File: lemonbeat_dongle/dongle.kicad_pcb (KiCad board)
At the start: 4 copper layers, 50 x 20 mm, 82 parts, among them J201 USB_A, J202 Prog, J203 u.FL, J301 SMA, SW201 SW_Push, U201 nRF52840, U301 Si4467, Y201 32MHz, Y202 32.768kHz, Y301 26MHz

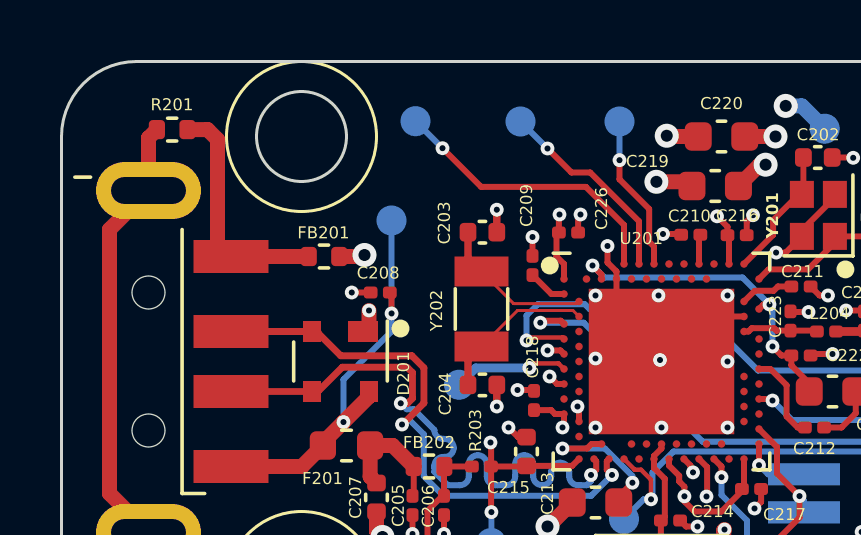
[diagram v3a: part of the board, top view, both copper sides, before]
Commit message: dongle: PCB: move test points away from hole
- move TP203 & TP206 away from hole (dongle & microjig)
- move TP205 away from TP206 (dongle & microjig)

Having the test points further away from the holes avoids shortcuts when
using a metal case & leaves space on the microjig for a nut.
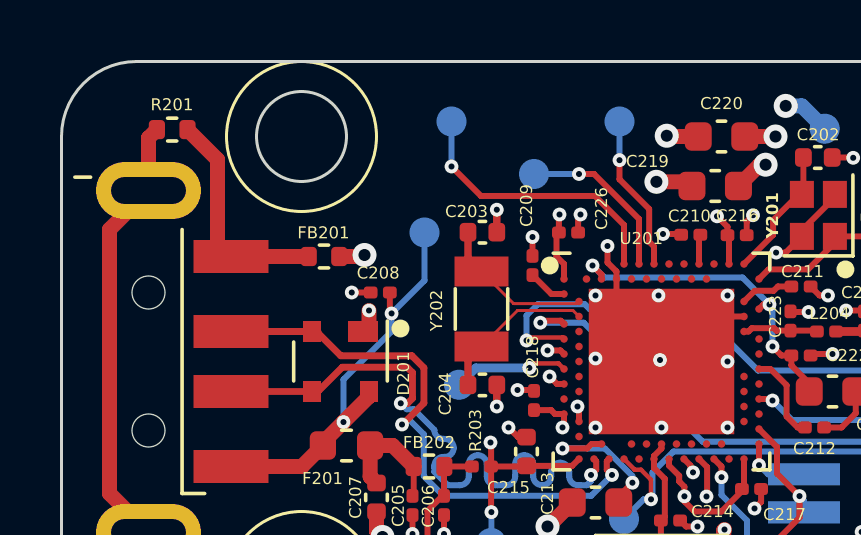
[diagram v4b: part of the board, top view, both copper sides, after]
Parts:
- moved TP205 1.81 mm to (126.2, 97.8)
- moved TP206 1.20 mm to (123.5, 96.0)
- moved TP203 1.17 mm to (122.6, 99.7)
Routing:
- net Net-(U201-AIN5/P0.29): track 6.75 -> 5.62 mm
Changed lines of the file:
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@@
     (property "ki_keywords" "cap capacitor")
     (attr smd)
-    (fp_text reference "C203" (at 1.27 0.31 270) (layer "F.SilkS")
+    (fp_text reference "C203" (at 0.53 0.69) (layer "F.SilkS")
         (effects (font (size 0.4 0.4) (thickness 0.1)))
     )
@@
   )
   (footprint "TestPoint:TestPoint_Pad_D1.0mm" (layer "B.Cu")
-    (at 125.8 96 180)
+    (at 126.25 97.75 180)
     (descr "SMD pad as test Point, diameter 1.0mm")
     (tags "test point SMD pad")
@@
   )
   (footprint "TestPoint:TestPoint_Pad_D1.0mm" (layer "B.Cu")
-    (at 121.5 99.3 180)
+    (at 122.6 99.7 180)
     (descr "SMD pad as test Point, diameter 1.0mm")
     (tags "test point SMD pad")
@@
   )
   (footprint "TestPoint:TestPoint_Pad_D1.0mm" (layer "B.Cu")
-    (at 122.3 95.99 180)
+    (at 123.5 96 180)
     (descr "SMD pad as test Point, diameter 1.0mm")
     (tags "test point SMD pad")
@@
   (segment (start 120.75 105) (end 120.75 105.167408) (width 0.5) (layer "F.Cu") (net 8))
   (segment (start 116.35 107.5) (end 118.5125 107.5) (width 0.5) (layer "F.Cu") (net 8))
-  (segment (start 121.502085 101.862085) (end 121.39 101.75) (width 0.2) (layer "F.Cu") (net 8))
-  (segment (start 121.502085 102.397915) (end 121.502085 101.862085) (width 0.2) (layer "F.Cu") (net 8))
   (segment (start 120.75 105.167408) (end 119.89912 106.018288) (width 0.5) (layer "F.Cu") (net 8))
   (segment (start 119.2125 106.704908) (end 119.89912 106.018288) (width 0.5) (layer "F.Cu") (net 8))
   (segment (start 118.5125 107.5) (end 119.2125 106.8) (width 0.5) (layer "F.Cu") (net 8))
+  (segment (start 121.445 101.7) (end 121.445 102.34083) (width 0.2) (layer "F.Cu") (net 8))
+  (segment (start 121.445 102.34083) (end 121.502085 102.397915) (width 0.2) (layer "F.Cu") (net 8))
   (via (at 119.89912 106.018288) (size 0.46) (drill 0.2) (layers "F.Cu" "B.Cu") (net 8))
   (via (at 121.502085 102.397915) (size 0.46) (drill 0.2) (layers "F.Cu" "B.Cu") (net 8))
-  (segment (start 121.502085 102.397915) (end 121.502085 102.997915) (width 0.2) (layer "B.Cu") (net 8))
-  (segment (start 119.89912 104.60088) (end 119.89912 106.018288) (width 0.2) (layer "B.Cu") (net 8))
   (segment (start 121.502085 102.997915) (end 119.89912 104.60088) (width 0.2) (layer "B.Cu") (net 8))
-  (segment (start 121.5 102.39583) (end 121.5 99.3) (width 0.2) (layer "B.Cu") (net 8))
-  (segment (start 121.502085 102.397915) (end 121.5 102.39583) (width 0.2) (layer "B.Cu") (net 8))
+  (segment (start 121.502085 102.997915) (end 121.502085 102.397915) (width 0.2) (layer "B.Cu") (net 8))
+  (segment (start 121.502085 102.397915) (end 122.6 101.3) (width 0.2) (layer "B.Cu") (net 8))
+  (segment (start 119.89912 104.60088) (end 119.89912 106.018288) (width 0.2) (layer "B.Cu") (net 8))
+  (segment (start 122.6 101.3) (end 122.6 99.7) (width 0.2) (layer "B.Cu") (net 8))
   (segment (start 126.83 101.75) (end 126.2 101.12) (width 0.2) (layer "F.Cu") (net 9))
   (segment (start 127.25 101.75) (end 126.83 101.75) (width 0.2) (layer "F.Cu") (net 9))
@@
   (segment (start 144.5375 111.4) (end 144.5375 110.2725) (width 0.2) (layer "F.Cu") (net 33))
   (segment (start 144.5375 110.2725) (end 144.9 109.91) (width 0.2) (layer "F.Cu") (net 33))
-  (segment (start 114.7 96.27) (end 115.37 96.27) (width 0.5) (layer "F.Cu") (net 34))
-  (segment (start 116.35 100.5) (end 118.1 100.5) (width 0.5) (layer "F.Cu") (net 34))
   (segment (start 115.7 100.05) (end 116.15 100.5) (width 0.5) (layer "F.Cu") (net 34))
-  (segment (start 115.7 96.6) (end 115.7 100.05) (width 0.5) (layer "F.Cu") (net 34))
-  (segment (start 115.37 96.27) (end 115.7 96.6) (width 0.5) (layer "F.Cu") (net 34))
+  (segment (start 116.35 100.5) (end 118.1 100.5) (width 0.5) (layer "F.Cu") (net 34))
+  (segment (start 115.7 97.27) (end 115.7 100.05) (width 0.5) (layer "F.Cu") (net 34))
   (segment (start 118.1 100.5) (end 118.74 100.5) (width 0.5) (layer "F.Cu") (net 34))
+  (segment (start 114.7 96.27) (end 115.7 97.27) (width 0.5) (layer "F.Cu") (net 34))
   (segment (start 112.1 99.6) (end 113.4 98.3) (width 0.5) (layer "F.Cu") (net 35))
   (segment (start 113.4 109.7) (end 112.1 108.4) (width 0.5) (layer "F.Cu") (net 35))
@@
   (segment (start 129.1 97.29) (end 129.1 96) (width 0.2) (layer "B.Cu") (net 48))
   (segment (start 129.75 99.327552) (end 129.75 100.75) (width 0.2) (layer "F.Cu") (net 49))
-  (segment (start 128.122448 97.7) (end 129.75 99.327552) (width 0.2) (layer "F.Cu") (net 49))
-  (segment (start 126.7 96.9) (end 127.5 97.7) (width 0.2) (layer "F.Cu") (net 49))
-  (segment (start 127.5 97.7) (end 128.122448 97.7) (width 0.2) (layer "F.Cu") (net 49))
-  (via (at 126.7 96.9) (size 0.46) (drill 0.2) (layers "F.Cu" "B.Cu") (net 49))
-  (segment (start 126.7 96.9) (end 125.8 96) (width 0.2) (layer "B.Cu") (net 49))
+  (segment (start 129.75 99.25) (end 128.25 97.75) (width 0.2) (layer "F.Cu") (net 49))
+  (segment (start 129.75 99.327552) (end 129.75 99.25) (width 0.2) (layer "F.Cu") (net 49))
+  (segment (start 128.25 97.75) (end 127.75 97.75) (width 0.2) (layer "F.Cu") (net 49))
+  (via (at 127.75 97.75) (size 0.46) (drill 0.2) (layers "F.Cu" "B.Cu") (net 49))
+  (segment (start 127.75 97.75) (end 126.25 97.75) (width 0.2) (layer "B.Cu") (net 49))
   (segment (start 129.25 99.45) (end 129.25 100.75) (width 0.2) (layer "F.Cu") (net 50))
-  (segment (start 127.98 98.18) (end 129.25 99.45) (width 0.2) (layer "F.Cu") (net 50))
-  (segment (start 123.2 96.89) (end 124.49 98.18) (width 0.2) (layer "F.Cu") (net 50))
-  (segment (start 124.49 98.18) (end 127.98 98.18) (width 0.2) (layer "F.Cu") (net 50))
-  (via (at 123.2 96.89) (size 0.46) (drill 0.2) (layers "F.Cu" "B.Cu") (net 50))
-  (segment (start 123.2 96.89) (end 122.3 95.99) (width 0.2) (layer "B.Cu") (net 50))
+  (segment (start 124.483 98.483) (end 123.5 97.5) (width 0.2) (layer "F.Cu") (net 50))
+  (segment (start 128.283 98.483) (end 124.483 98.483) (width 0.2) (layer "F.Cu") (net 50))
+  (segment (start 129.25 99.45) (end 128.283 98.483) (width 0.2) (layer "F.Cu") (net 50))
+  (via (at 123.5 97.5) (size 0.46) (drill 0.2) (layers "F.Cu" "B.Cu") (net 50))
+  (segment (start 123.5 97.5) (end 123.5 96) (width 0.2) (layer "B.Cu") (net 50))
   (segment (start 141.7875 106.375) (end 141.221 106.375) (width 0.2) (layer "F.Cu") (net 86))
   (segment (start 140.373 107.223) (end 140.373 108.923) (width 0.2) (layer "F.Cu") (net 86))

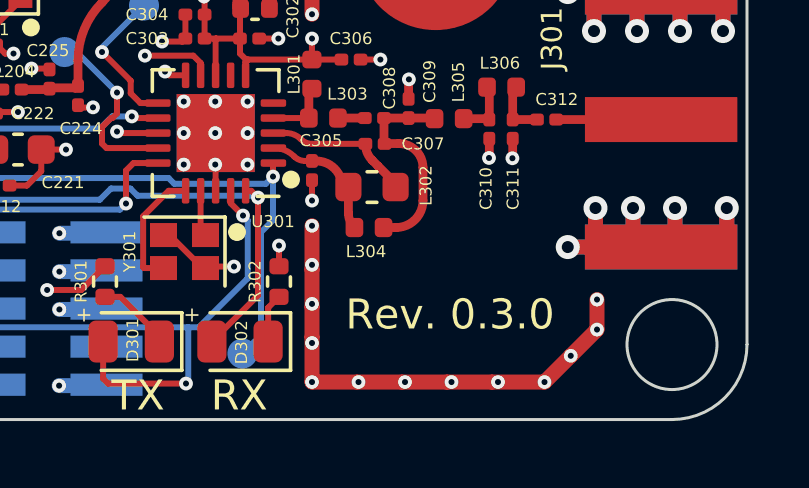
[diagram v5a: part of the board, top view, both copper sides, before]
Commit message: dongle & micro jig: increase revision to 0.4.0 everywhere
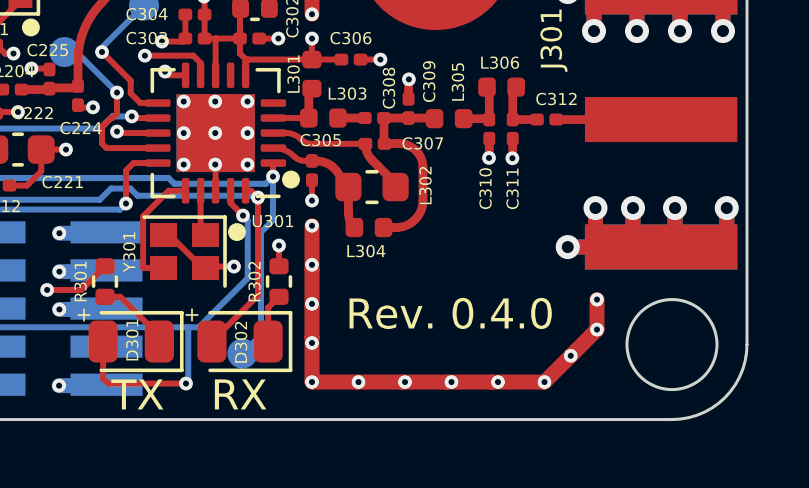
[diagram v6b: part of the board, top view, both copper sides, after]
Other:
- board text added: "Rev. 0.4.0"
- board text removed: "Rev. 0.3.0"
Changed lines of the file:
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@@
     (effects (font (size 0.5 0.5) (thickness 0.1)))
   )
-  (gr_text "Rev. 0.3.0" (at 150.6 110.5) (layer "F.SilkS")
+  (gr_text "Rev. 0.4.0" (at 150.6 110.5) (layer "F.SilkS")
     (effects (font (size 1 1) (thickness 0.15)))
   )

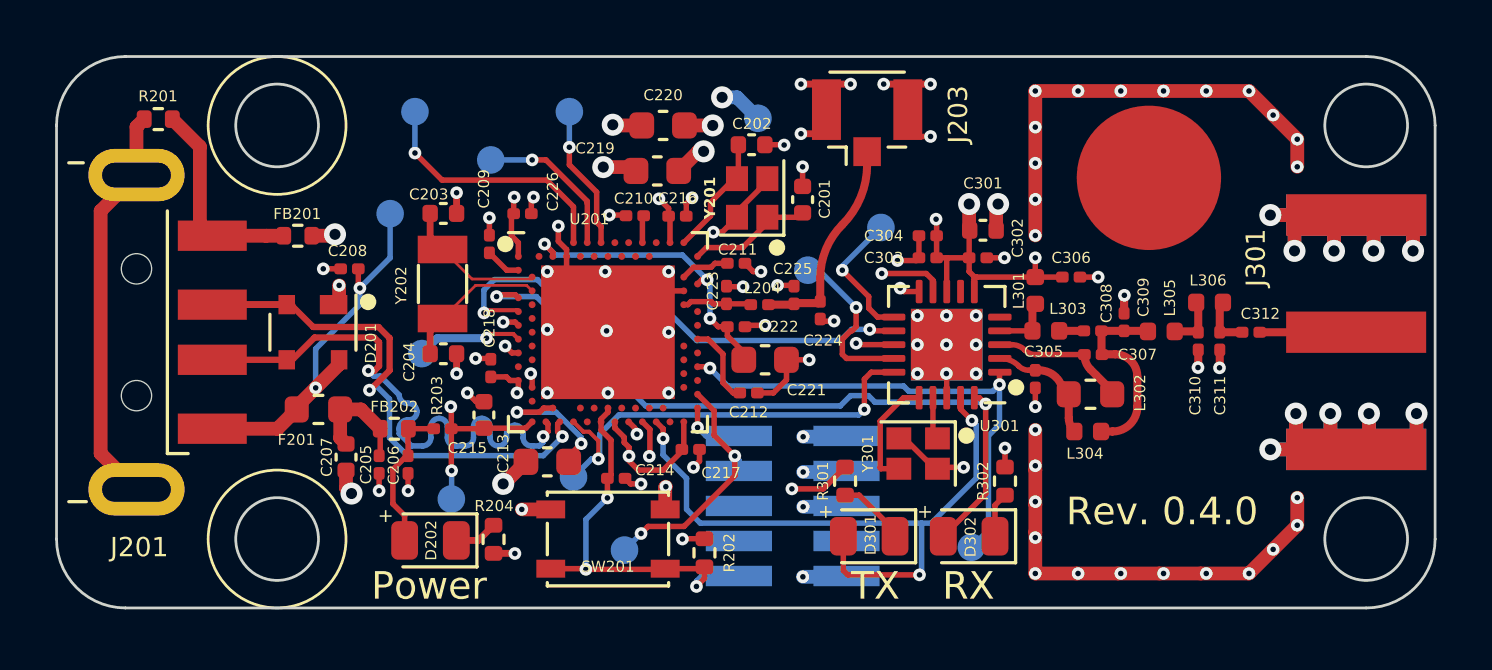
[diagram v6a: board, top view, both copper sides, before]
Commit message: dongle: schematic & PCB: add button
The existing button is connected to reset. This adds a second button
connected to P1.15, which can be used for user input (e.g. to enter the
boot loader on power on).
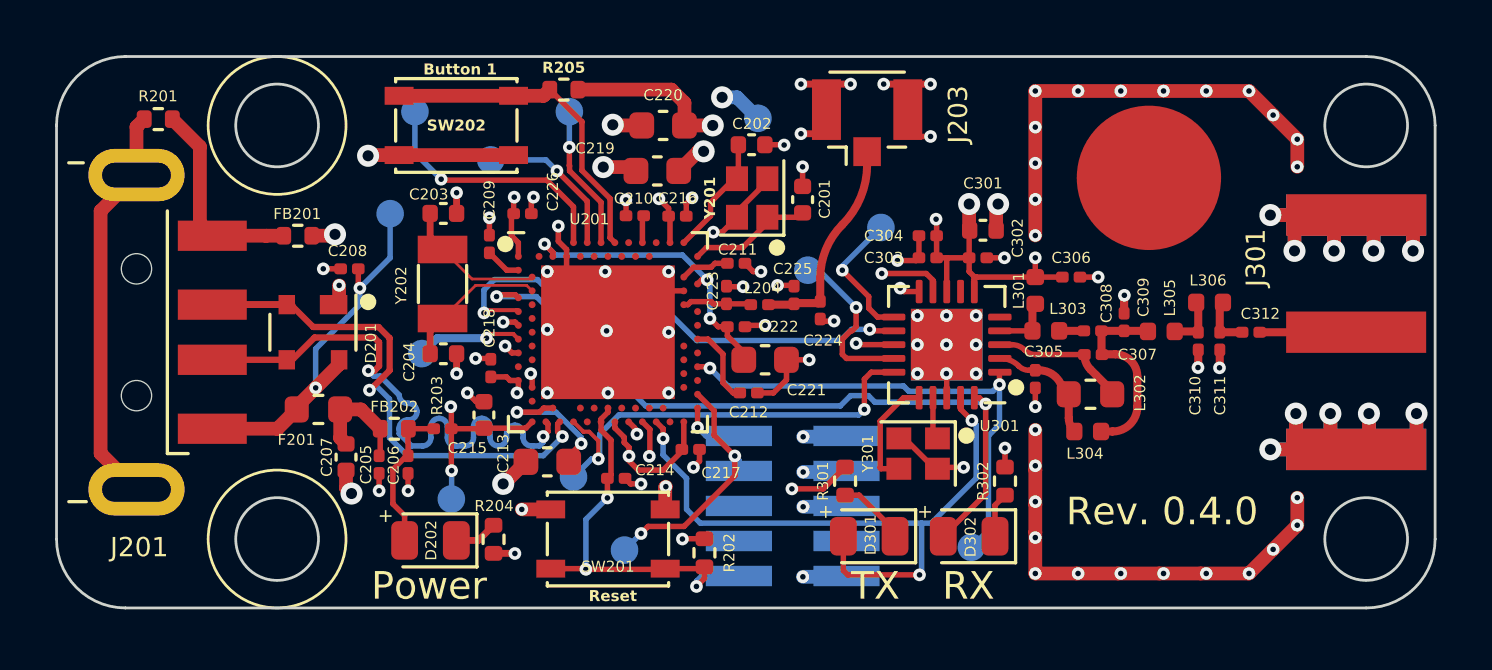
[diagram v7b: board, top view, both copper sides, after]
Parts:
- added R205: 10k, Resistor_SMD:R_0402_1005Metric, F.Cu at (128.9, 95.2)
- added SW202: SW_Push, Button_Switch_SMD:SW_SPST_PTS810, F.Cu at (125.0, 96.5)
- C201, C202: value 12pF -> 13pF
- C203, C204: value 12pF -> 22pF
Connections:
- U201 pad A14: unconnected-(U201-P1.15-PadA14) -> Net-(U201-P1.15)
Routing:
- net Net-(U201-P1.15): track 0.00 -> 12.1 mm
- net VDD: track 28.0 -> 33.2 mm, vias 12 -> 13
- net GND: track 120.8 -> 125.6 mm
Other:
- board text added: "Button 1"
- board text added: "Reset"
